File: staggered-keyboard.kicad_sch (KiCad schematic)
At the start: 129 parts

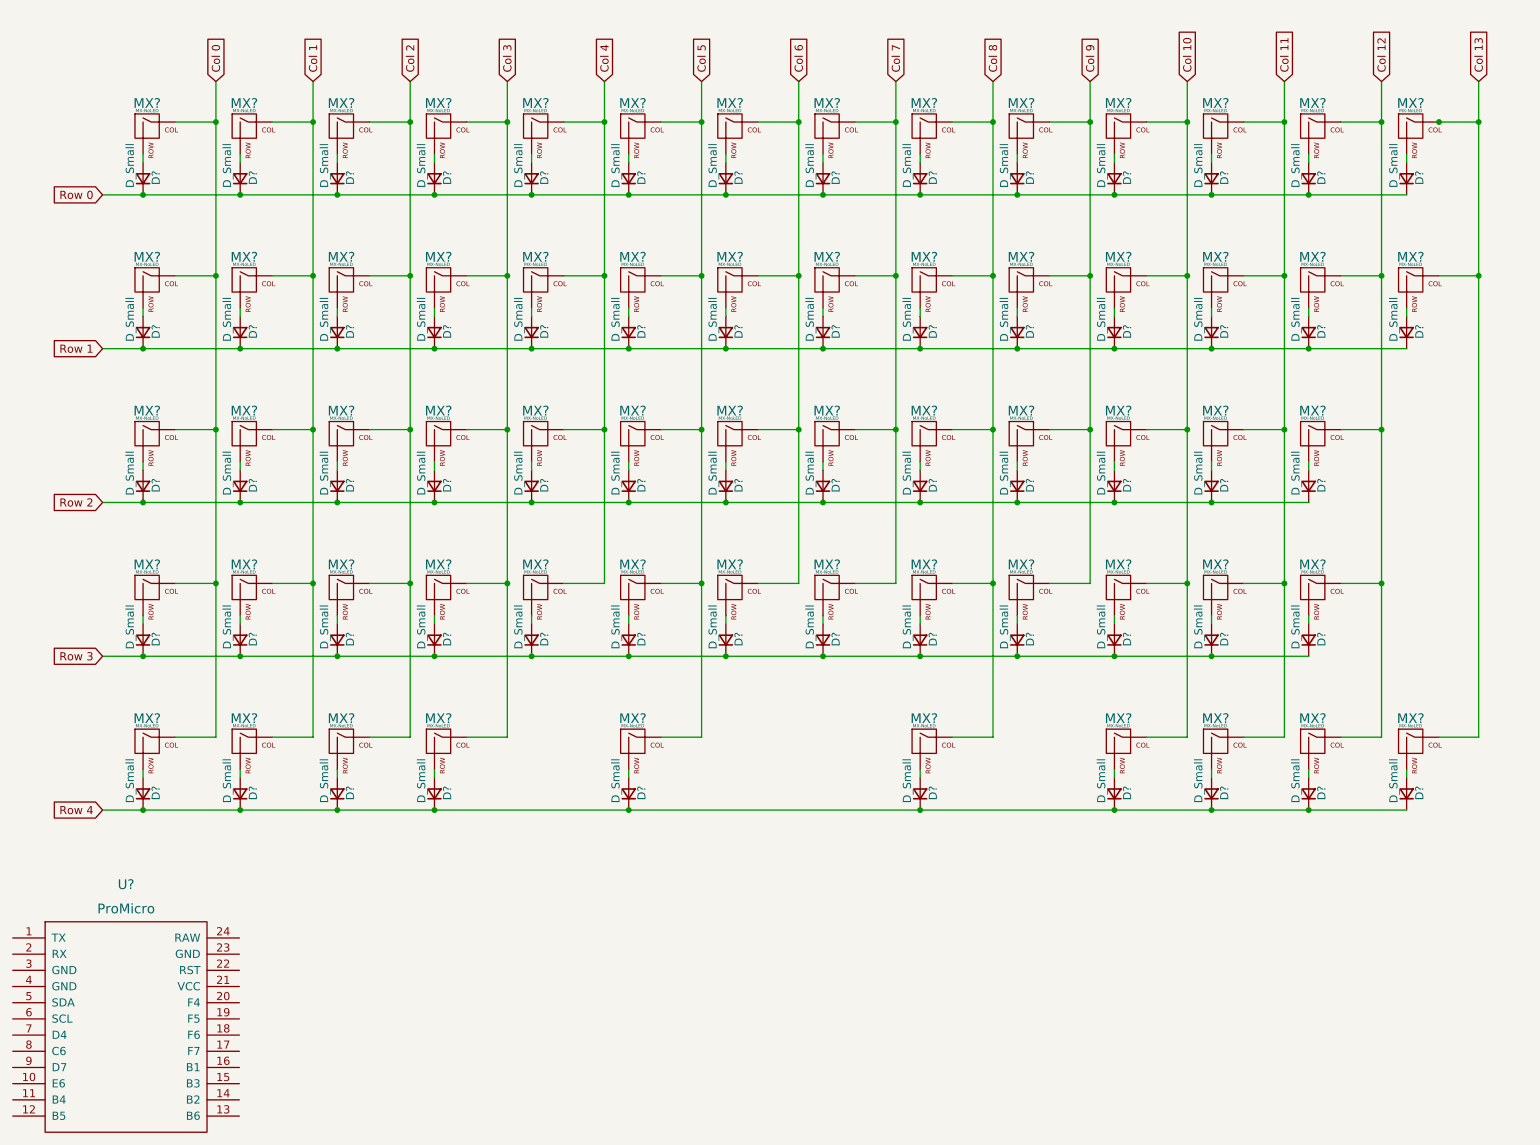
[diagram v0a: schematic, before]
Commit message: Place switches on pcb & fix footprint on schematic
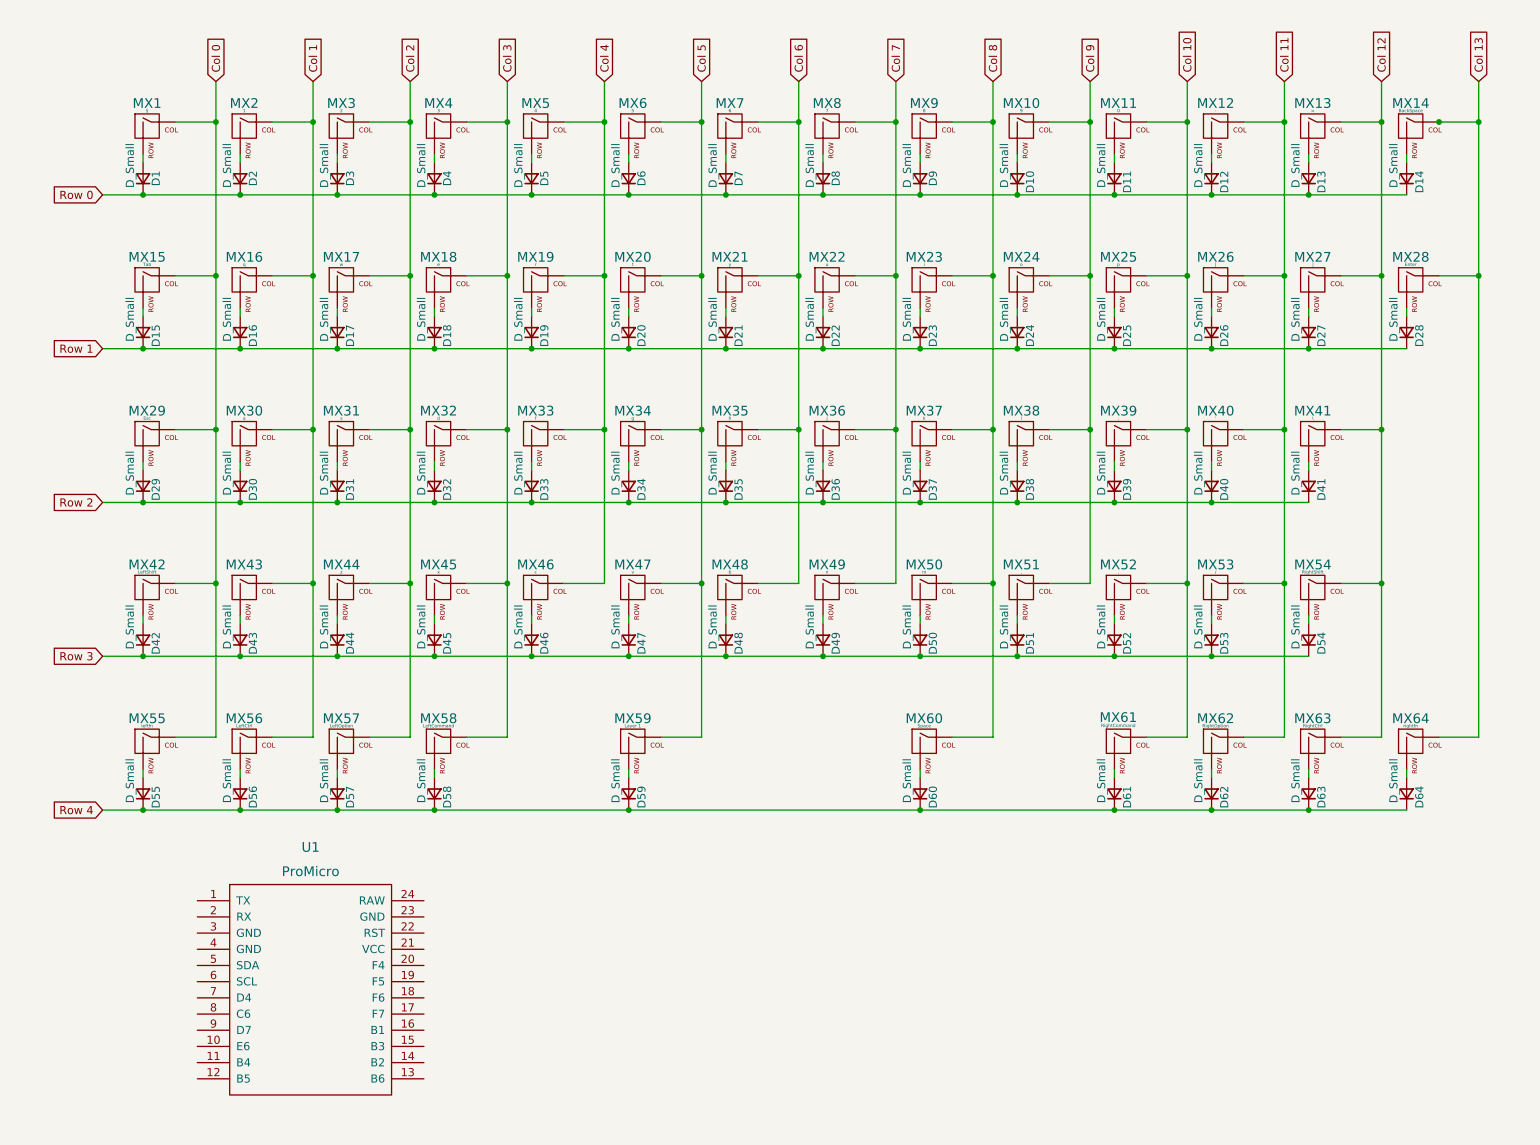
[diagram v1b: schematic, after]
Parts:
- D1, D10, D11, D12, D13, D14, D15, D16, D17, D18, D19, D2, D20, D21, D22, D23, D24, D25, D26, D27, D28, D29, D3, D30, D31, D32, D33, D34, D35, D36, D37, D38, D39, D4, D40, D41, D42, D43, D44, D45, D46, D47, D48, D49, D5, D50, D51, D52, D53, D54, D55, D56, D57, D58, D59, D6, D60, D61, D62, D63, D64, D7, D8, D9: renamed from D?; footprint (none) -> Diode_SMD:D_SOD-123
- MX1: renamed from MX?; value MX-NoLED -> §; footprint (none) -> Button_Switch_Keyboard:SW_Cherry_MX_1.00u_PCB
- MX10: renamed from MX?; value MX-NoLED -> 9; footprint (none) -> Button_Switch_Keyboard:SW_Cherry_MX_1.00u_PCB
- MX11: renamed from MX?; value MX-NoLED -> 0; footprint (none) -> Button_Switch_Keyboard:SW_Cherry_MX_1.00u_PCB
- MX12: renamed from MX?; value MX-NoLED -> -; footprint (none) -> Button_Switch_Keyboard:SW_Cherry_MX_1.00u_PCB
- MX13: renamed from MX?; value MX-NoLED -> =; footprint (none) -> Button_Switch_Keyboard:SW_Cherry_MX_1.00u_PCB
- MX14: renamed from MX?; value MX-NoLED -> BackSpace; footprint (none) -> Button_Switch_Keyboard:SW_Cherry_MX_2.00u_PCB
- MX15: renamed from MX?; value MX-NoLED -> Tab; footprint (none) -> Button_Switch_Keyboard:SW_Cherry_MX_1.50u_PCB
- MX16: renamed from MX?; value MX-NoLED -> q; footprint (none) -> Button_Switch_Keyboard:SW_Cherry_MX_1.00u_PCB
- MX17: renamed from MX?; value MX-NoLED -> w; footprint (none) -> Button_Switch_Keyboard:SW_Cherry_MX_1.00u_PCB
- MX18: renamed from MX?; value MX-NoLED -> e; footprint (none) -> Button_Switch_Keyboard:SW_Cherry_MX_1.00u_PCB
- MX19: renamed from MX?; value MX-NoLED -> r; footprint (none) -> Button_Switch_Keyboard:SW_Cherry_MX_1.00u_PCB
- MX2: renamed from MX?; value MX-NoLED -> 1; footprint (none) -> Button_Switch_Keyboard:SW_Cherry_MX_1.00u_PCB
- MX20: renamed from MX?; value MX-NoLED -> t; footprint (none) -> Button_Switch_Keyboard:SW_Cherry_MX_1.00u_PCB
- MX21: renamed from MX?; value MX-NoLED -> y; footprint (none) -> Button_Switch_Keyboard:SW_Cherry_MX_1.00u_PCB
- MX22: renamed from MX?; value MX-NoLED -> u; footprint (none) -> Button_Switch_Keyboard:SW_Cherry_MX_1.00u_PCB
- MX23: renamed from MX?; value MX-NoLED -> i; footprint (none) -> Button_Switch_Keyboard:SW_Cherry_MX_1.00u_PCB
- MX24: renamed from MX?; value MX-NoLED -> o; footprint (none) -> Button_Switch_Keyboard:SW_Cherry_MX_1.00u_PCB
- MX25: renamed from MX?; value MX-NoLED -> p; footprint (none) -> Button_Switch_Keyboard:SW_Cherry_MX_1.00u_PCB
- MX26: renamed from MX?; value MX-NoLED -> [; footprint (none) -> Button_Switch_Keyboard:SW_Cherry_MX_1.00u_PCB
- MX27: renamed from MX?; value MX-NoLED -> ]; footprint (none) -> Button_Switch_Keyboard:SW_Cherry_MX_1.00u_PCB
- MX28: renamed from MX?; value MX-NoLED -> Enter; footprint (none) -> Button_Switch_Keyboard:SW_Cherry_MX_ISOEnter_PCB
- MX29: renamed from MX?; value MX-NoLED -> Esc; footprint (none) -> MX_Only:MXOnly-1.75U-NoLED
- MX3: renamed from MX?; value MX-NoLED -> 2; footprint (none) -> Button_Switch_Keyboard:SW_Cherry_MX_1.00u_PCB
- MX30: renamed from MX?; value MX-NoLED -> a; footprint (none) -> Button_Switch_Keyboard:SW_Cherry_MX_1.00u_PCB
- MX31: renamed from MX?; value MX-NoLED -> s; footprint (none) -> Button_Switch_Keyboard:SW_Cherry_MX_1.00u_PCB
- MX32: renamed from MX?; value MX-NoLED -> d; footprint (none) -> Button_Switch_Keyboard:SW_Cherry_MX_1.00u_PCB
- MX33: renamed from MX?; value MX-NoLED -> f; footprint (none) -> Button_Switch_Keyboard:SW_Cherry_MX_1.00u_PCB
- MX34: renamed from MX?; value MX-NoLED -> g; footprint (none) -> Button_Switch_Keyboard:SW_Cherry_MX_1.00u_PCB
- MX35: renamed from MX?; value MX-NoLED -> h; footprint (none) -> Button_Switch_Keyboard:SW_Cherry_MX_1.00u_PCB
- MX36: renamed from MX?; value MX-NoLED -> j; footprint (none) -> Button_Switch_Keyboard:SW_Cherry_MX_1.00u_PCB
- MX37: renamed from MX?; value MX-NoLED -> k; footprint (none) -> Button_Switch_Keyboard:SW_Cherry_MX_1.00u_PCB
- MX38: renamed from MX?; value MX-NoLED -> l; footprint (none) -> Button_Switch_Keyboard:SW_Cherry_MX_1.00u_PCB
- MX39: renamed from MX?; value MX-NoLED -> ;; footprint (none) -> Button_Switch_Keyboard:SW_Cherry_MX_1.00u_PCB
- MX4: renamed from MX?; value MX-NoLED -> 3; footprint (none) -> Button_Switch_Keyboard:SW_Cherry_MX_1.00u_PCB
- MX40: renamed from MX?; value MX-NoLED -> '; footprint (none) -> Button_Switch_Keyboard:SW_Cherry_MX_1.00u_PCB
- MX41: renamed from MX?; value MX-NoLED -> \; footprint (none) -> Button_Switch_Keyboard:SW_Cherry_MX_1.00u_PCB
- MX42: renamed from MX?; value MX-NoLED -> LeftShift; footprint (none) -> MX_Only:MXOnly-1.25U-NoLED
- MX43: renamed from MX?; value MX-NoLED -> `; footprint (none) -> Button_Switch_Keyboard:SW_Cherry_MX_1.00u_PCB
- MX44: renamed from MX?; value MX-NoLED -> z; footprint (none) -> Button_Switch_Keyboard:SW_Cherry_MX_1.00u_PCB
- MX45: renamed from MX?; value MX-NoLED -> x; footprint (none) -> Button_Switch_Keyboard:SW_Cherry_MX_1.00u_PCB
- MX46: renamed from MX?; value MX-NoLED -> c; footprint (none) -> Button_Switch_Keyboard:SW_Cherry_MX_1.00u_PCB
- MX47: renamed from MX?; value MX-NoLED -> v; footprint (none) -> Button_Switch_Keyboard:SW_Cherry_MX_1.00u_PCB
- MX48: renamed from MX?; value MX-NoLED -> b; footprint (none) -> Button_Switch_Keyboard:SW_Cherry_MX_1.00u_PCB
- MX49: renamed from MX?; value MX-NoLED -> n; footprint (none) -> Button_Switch_Keyboard:SW_Cherry_MX_1.00u_PCB
- MX5: renamed from MX?; value MX-NoLED -> 4; footprint (none) -> Button_Switch_Keyboard:SW_Cherry_MX_1.00u_PCB
- MX50: renamed from MX?; value MX-NoLED -> m; footprint (none) -> Button_Switch_Keyboard:SW_Cherry_MX_1.00u_PCB
- MX51: renamed from MX?; value MX-NoLED -> ,; footprint (none) -> Button_Switch_Keyboard:SW_Cherry_MX_1.00u_PCB
- MX52: renamed from MX?; value MX-NoLED -> .; footprint (none) -> Button_Switch_Keyboard:SW_Cherry_MX_1.00u_PCB
- MX53: renamed from MX?; value MX-NoLED -> /; footprint (none) -> Button_Switch_Keyboard:SW_Cherry_MX_1.00u_PCB
- MX54: renamed from MX?; value MX-NoLED -> RightShift; footprint (none) -> MX_Only:MXOnly-2.75U-NoLED
- MX55: renamed from MX?; value MX-NoLED -> leftfn; footprint (none) -> MX_Only:MXOnly-1U-NoLED
- MX56: renamed from MX?; value MX-NoLED -> LeftCtrl; footprint (none) -> MX_Only:MXOnly-1.25U-NoLED
- MX57: renamed from MX?; value MX-NoLED -> LeftOption; footprint (none) -> MX_Only:MXOnly-1.25U-NoLED
- MX58: renamed from MX?; value MX-NoLED -> LeftCommand; footprint (none) -> MX_Only:MXOnly-1.25U-NoLED
- MX59: renamed from MX?; value MX-NoLED -> Layer 1; footprint (none) -> MX_Only:MXOnly-2.75U-NoLED
- MX6: renamed from MX?; value MX-NoLED -> 5; footprint (none) -> Button_Switch_Keyboard:SW_Cherry_MX_1.00u_PCB
- MX60: renamed from MX?; value MX-NoLED -> Space; footprint (none) -> MX_Only:MXOnly-2.75U-NoLED
- MX61: renamed from MX?; value MX-NoLED -> RightCommand; footprint (none) -> MX_Only:MXOnly-1.25U-NoLED
- MX62: renamed from MX?; value MX-NoLED -> RightOption; footprint (none) -> MX_Only:MXOnly-1.25U-NoLED
- MX63: renamed from MX?; value MX-NoLED -> RightCtrl; footprint (none) -> MX_Only:MXOnly-1.25U-NoLED
- MX64: renamed from MX?; value MX-NoLED -> rightfn; footprint (none) -> MX_Only:MXOnly-1U-NoLED
- MX7: renamed from MX?; value MX-NoLED -> 6; footprint (none) -> Button_Switch_Keyboard:SW_Cherry_MX_1.00u_PCB
- MX8: renamed from MX?; value MX-NoLED -> 7; footprint (none) -> Button_Switch_Keyboard:SW_Cherry_MX_1.00u_PCB
- MX9: renamed from MX?; value MX-NoLED -> 8; footprint (none) -> Button_Switch_Keyboard:SW_Cherry_MX_1.00u_PCB
- U1: renamed from U?; footprint (none) -> promicro:ProMicro
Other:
- moved on the sheet: U1

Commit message: Update footprint for 1U switches & align diode for first row
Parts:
- MX1, MX10, MX11, MX12, MX13, MX16, MX17, MX18, MX19, MX2, MX20, MX21, MX22, MX23, MX24, MX25, MX26, MX27, MX3, MX30, MX31, MX32, MX33, MX34, MX35, MX36, MX37, MX38, MX39, MX4, MX40, MX41, MX43, MX44, MX45, MX46, MX47, MX48, MX49, MX5, MX50, MX51, MX52, MX53, MX6, MX7, MX8, MX9: footprint Button_Switch_Keyboard:SW_Cherry_MX_1.00u_PCB -> MX_Only:MXOnly-1U-NoLED
- MX14: footprint Button_Switch_Keyboard:SW_Cherry_MX_2.00u_PCB -> MX_Only:MXOnly-2U-NoLED
- MX15: footprint Button_Switch_Keyboard:SW_Cherry_MX_1.50u_PCB -> MX_Only:MXOnly-1.5U-NoLED
- MX28: footprint Button_Switch_Keyboard:SW_Cherry_MX_ISOEnter_PCB -> MX_Only:MXOnly-ISO-NoLED

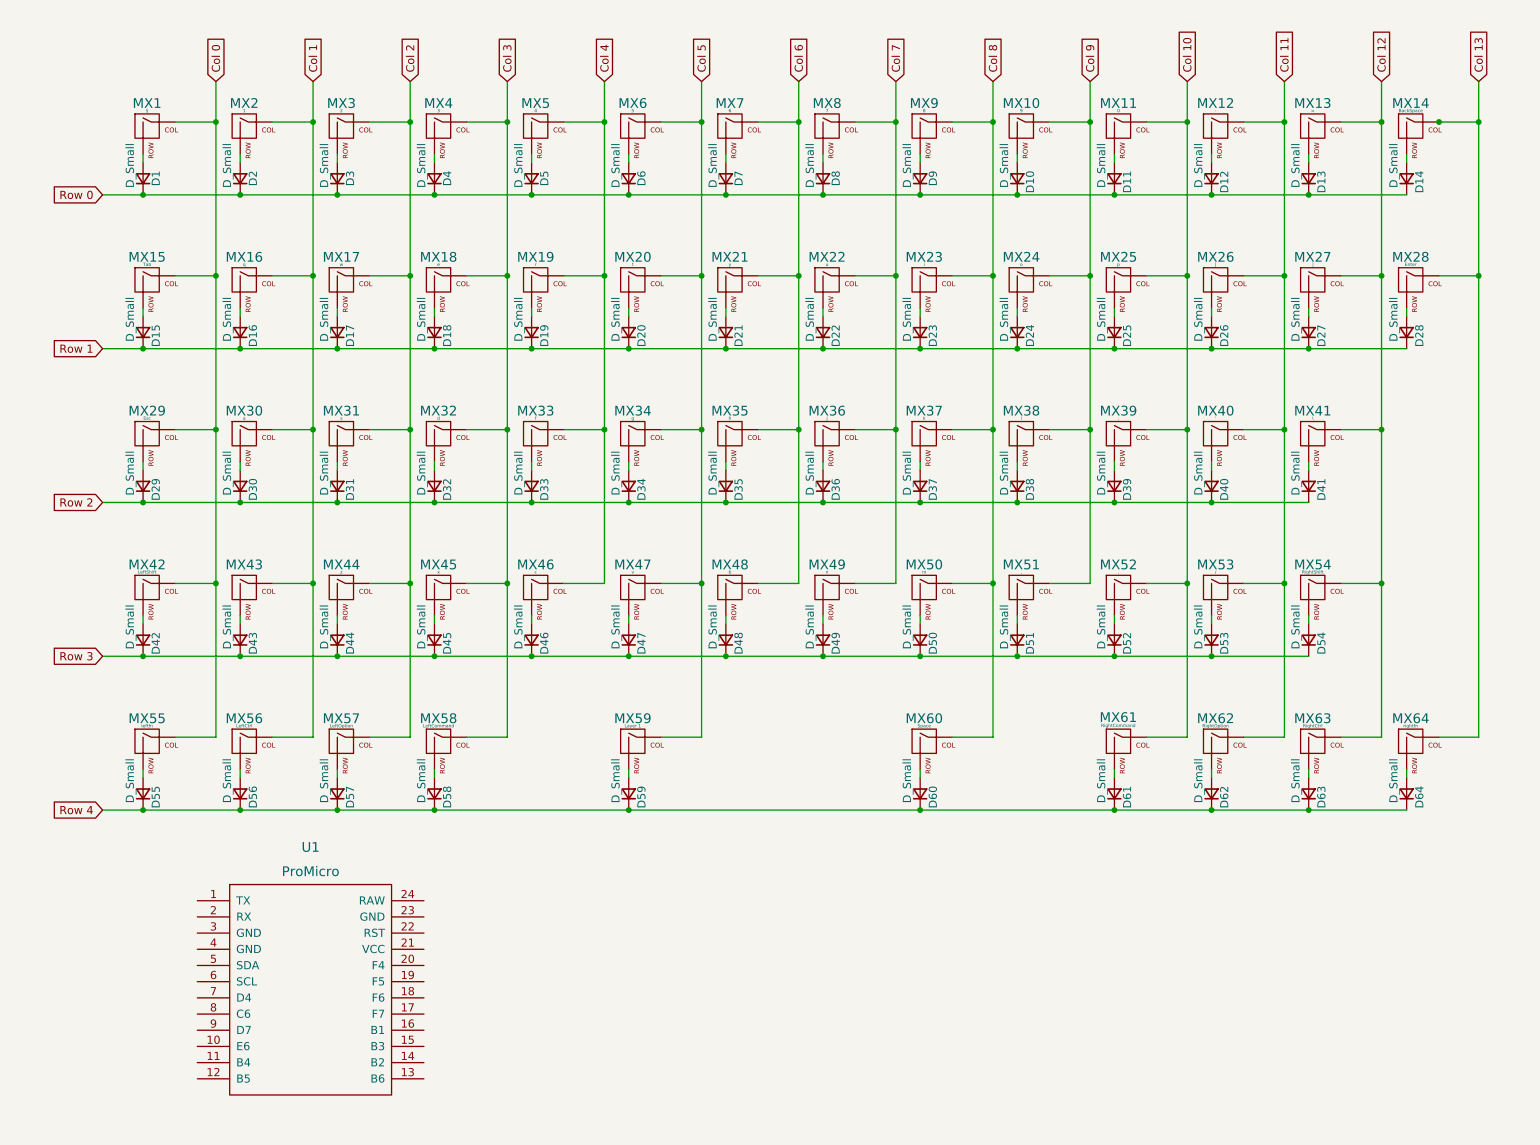
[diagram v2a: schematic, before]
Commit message: Finish routing of the pcb & update layout in schematic
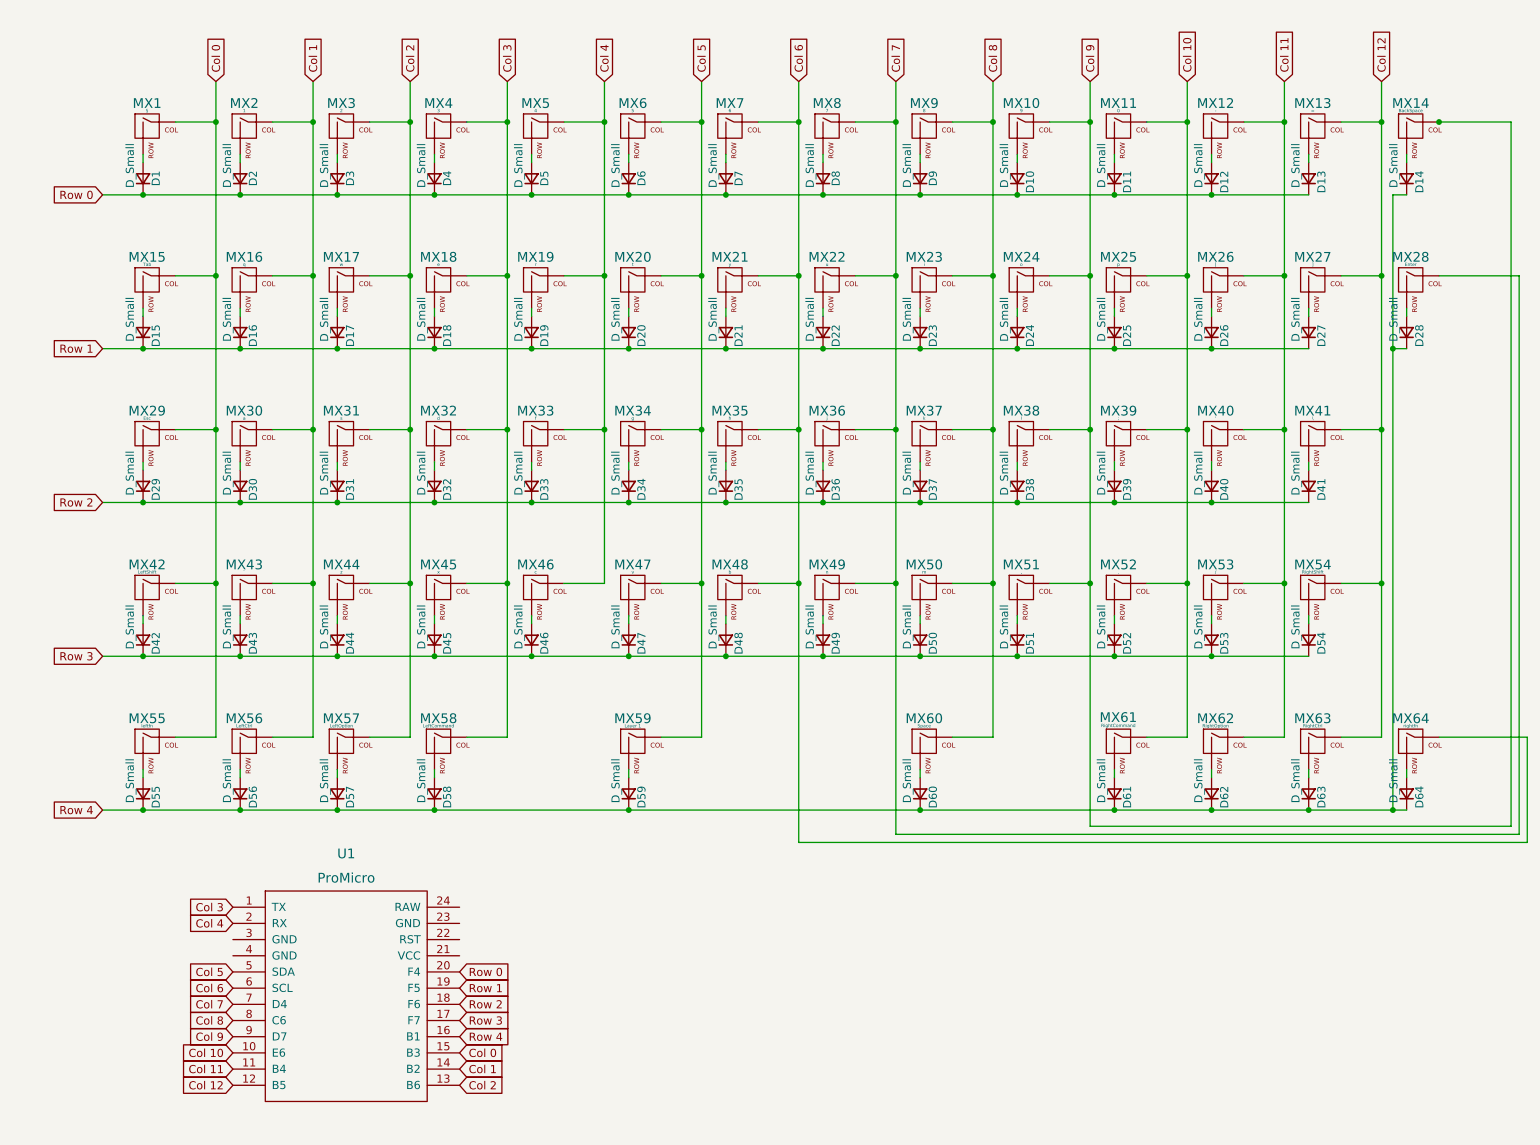
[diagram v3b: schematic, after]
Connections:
- net Col 0: now also U1.15 (B3)
- net Col 1: now also U1.14 (B2)
- net Col 10: now also U1.10 (E6)
- net Col 11: now also U1.11 (B4)
- net Col 12: now also U1.12 (B5)
- net Col 2: now also U1.13 (B6)
- net Col 3: now also U1.1 (TX)
- net Col 4: now also U1.2 (RX)
- net Col 5: now also U1.5 (SDA)
- net Col 6: now also MX64.1 (COL), U1.6 (SCL)
- net Col 7: now also MX28.1 (COL), U1.7 (D4)
- net Col 8: now also U1.8 (C6)
- net Col 9: now also MX14.1 (COL), U1.9 (D7)
- net Row 0: now also U1.20 (F4); no longer D14.1 (K)
- net Row 1: now also U1.19 (F5); no longer D28.1 (K)
- net Row 2: now also U1.18 (F6)
- net Row 3: now also U1.17 (F7)
- net Row 4: now also D14.1 (K), D28.1 (K), U1.16 (B1)
- removed net Col 13: MX14.1 (COL), MX28.1 (COL), MX64.1 (COL)
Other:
- moved on the sheet: U1
